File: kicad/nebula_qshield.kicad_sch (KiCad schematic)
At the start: 0 parts

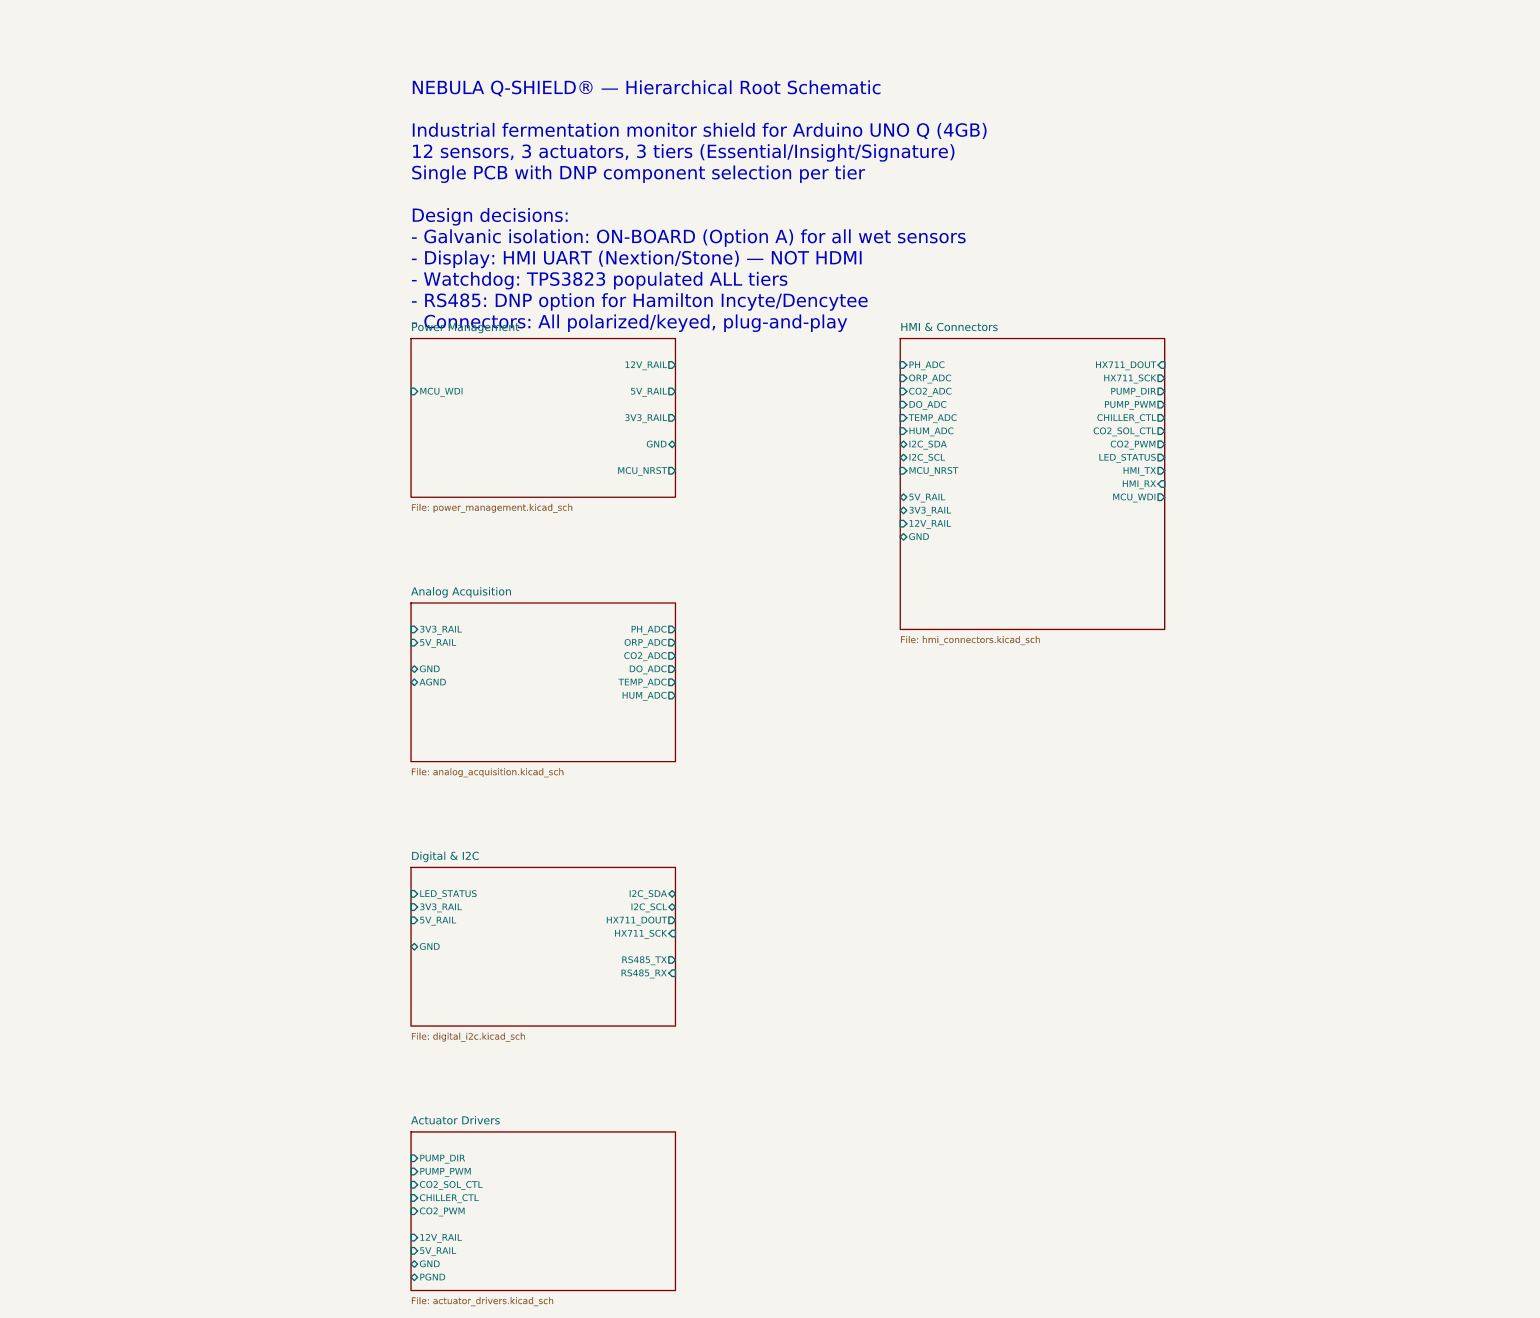
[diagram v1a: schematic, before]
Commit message: feat: Wire digital_i2c, actuator_drivers, hmi_connectors + root schematic — ERC violations 322→24 (acceptable)
Co-Authored-By: Devin AI <158243242+devin-ai-integration[bot]@users.noreply.github.com>
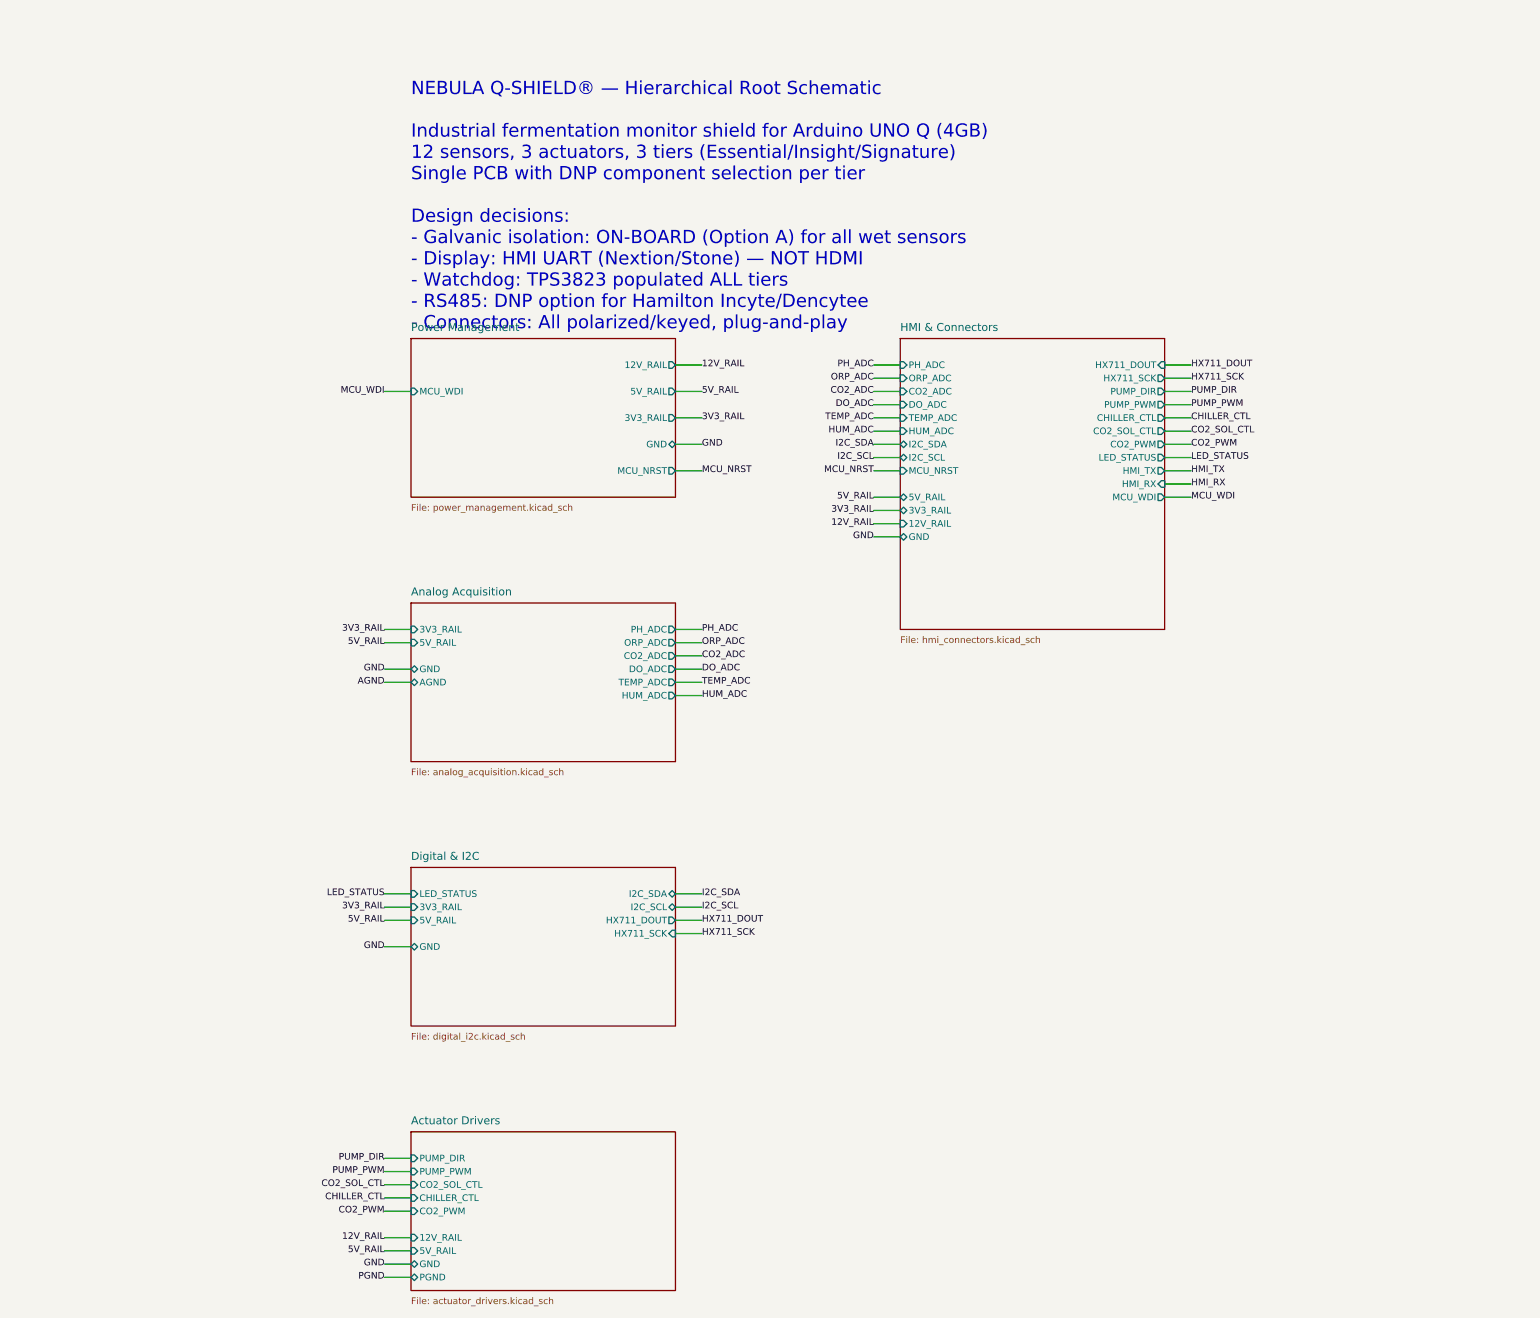
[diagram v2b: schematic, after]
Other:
- sheet Digital & I2C ports: added none; removed RS485_RX, RS485_TX
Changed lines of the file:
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@@
     (pin "HX711_SCK"  input       (at 76.2 165.1 0)     (effects (font (size 1.27 1.27))))
     (pin "LED_STATUS" input       (at 25.4 157.48 180)  (effects (font (size 1.27 1.27))))
-    (pin "RS485_TX"   output      (at 76.2 170.18 0)    (effects (font (size 1.27 1.27))))
-    (pin "RS485_RX"   input       (at 76.2 172.72 0)    (effects (font (size 1.27 1.27))))
     (pin "3V3_RAIL"   input       (at 25.4 160.02 180)  (effects (font (size 1.27 1.27))))
     (pin "5V_RAIL"    input       (at 25.4 162.56 180)  (effects (font (size 1.27 1.27))))
@@
     (effects (font (size 2.54 2.54)) (justify left))
   )
+  (wire (pts (xy 76.20 55.88) (xy 81.28 55.88)) (stroke (width 0) (type default)))
+  (label "12V_RAIL" (at 81.28 55.88 0) (effects (font (size 1.27 1.27))))
+  (wire (pts (xy 25.40 223.52) (xy 20.32 223.52)) (stroke (width 0) (type default)))
+  (label "12V_RAIL" (at 20.32 223.52 180) (effects (font (size 1.27 1.27))))
+  (wire (pts (xy 119.38 86.36) (xy 114.30 86.36)) (stroke (width 0) (type default)))
+  (label "12V_RAIL" (at 114.30 86.36 180) (effects (font (size 1.27 1.27))))
+  (wire (pts (xy 76.20 60.96) (xy 81.28 60.96)) (stroke (width 0) (type default)))
+  (label "5V_RAIL" (at 81.28 60.96 0) (effects (font (size 1.27 1.27))))
+  (wire (pts (xy 25.40 109.22) (xy 20.32 109.22)) (stroke (width 0) (type default)))
+  (label "5V_RAIL" (at 20.32 109.22 180) (effects (font (size 1.27 1.27))))
+  (wire (pts (xy 25.40 162.56) (xy 20.32 162.56)) (stroke (width 0) (type default)))
+  (label "5V_RAIL" (at 20.32 162.56 180) (effects (font (size 1.27 1.27))))
+  (wire (pts (xy 25.40 226.06) (xy 20.32 226.06)) (stroke (width 0) (type default)))
+  (label "5V_RAIL" (at 20.32 226.06 180) (effects (font (size 1.27 1.27))))
+  (wire (pts (xy 119.38 81.28) (xy 114.30 81.28)) (stroke (width 0) (type default)))
+  (label "5V_RAIL" (at 114.30 81.28 180) (effects (font (size 1.27 1.27))))
+  (wire (pts (xy 76.20 66.04) (xy 81.28 66.04)) (stroke (width 0) (type default)))
+  (label "3V3_RAIL" (at 81.28 66.04 0) (effects (font (size 1.27 1.27))))
+  (wire (pts (xy 25.40 106.68) (xy 20.32 106.68)) (stroke (width 0) (type default)))
+  (label "3V3_RAIL" (at 20.32 106.68 180) (effects (font (size 1.27 1.27))))
+  (wire (pts (xy 25.40 160.02) (xy 20.32 160.02)) (stroke (width 0) (type default)))
+  (label "3V3_RAIL" (at 20.32 160.02 180) (effects (font (size 1.27 1.27))))
+  (wire (pts (xy 119.38 83.82) (xy 114.30 83.82)) (stroke (width 0) (type default)))
+  (label "3V3_RAIL" (at 114.30 83.82 180) (effects (font (size 1.27 1.27))))
+  (wire (pts (xy 76.20 71.12) (xy 81.28 71.12)) (stroke (width 0) (type default)))
+  (label "GND" (at 81.28 71.12 0) (effects (font (size 1.27 1.27))))
+  (wire (pts (xy 25.40 114.30) (xy 20.32 114.30)) (stroke (width 0) (type default)))
+  (label "GND" (at 20.32 114.30 180) (effects (font (size 1.27 1.27))))
+  (wire (pts (xy 25.40 167.64) (xy 20.32 167.64)) (stroke (width 0) (type default)))
+  (label "GND" (at 20.32 167.64 180) (effects (font (size 1.27 1.27))))
+  (wire (pts (xy 25.40 228.60) (xy 20.32 228.60)) (stroke (width 0) (type default)))
+  (label "GND" (at 20.32 228.60 180) (effects (font (size 1.27 1.27))))
+  (wire (pts (xy 119.38 88.90) (xy 114.30 88.90)) (stroke (width 0) (type default)))
+  (label "GND" (at 114.30 88.90 180) (effects (font (size 1.27 1.27))))
+  (wire (pts (xy 25.40 231.14) (xy 20.32 231.14)) (stroke (width 0) (type default)))
+  (label "PGND" (at 20.32 231.14 180) (effects (font (size 1.27 1.27))))
+  (wire (pts (xy 25.40 116.84) (xy 20.32 116.84)) (stroke (width 0) (type default)))
+  (label "AGND" (at 20.32 116.84 180) (effects (font (size 1.27 1.27))))
+  (wire (pts (xy 76.20 106.68) (xy 81.28 106.68)) (stroke (width 0) (type default)))
+  (label "PH_ADC" (at 81.28 106.68 0) (effects (font (size 1.27 1.27))))
+  (wire (pts (xy 119.38 55.88) (xy 114.30 55.88)) (stroke (width 0) (type default)))
+  (label "PH_ADC" (at 114.30 55.88 180) (effects (font (size 1.27 1.27))))
+  (wire (pts (xy 76.20 109.22) (xy 81.28 109.22)) (stroke (width 0) (type default)))
+  (label "ORP_ADC" (at 81.28 109.22 0) (effects (font (size 1.27 1.27))))
+  (wire (pts (xy 119.38 58.42) (xy 114.30 58.42)) (stroke (width 0) (type default)))
+  (label "ORP_ADC" (at 114.30 58.42 180) (effects (font (size 1.27 1.27))))
+  (wire (pts (xy 76.20 111.76) (xy 81.28 111.76)) (stroke (width 0) (type default)))
+  (label "CO2_ADC" (at 81.28 111.76 0) (effects (font (size 1.27 1.27))))
+  (wire (pts (xy 119.38 60.96) (xy 114.30 60.96)) (stroke (width 0) (type default)))
+  (label "CO2_ADC" (at 114.30 60.96 180) (effects (font (size 1.27 1.27))))
+  (wire (pts (xy 76.20 114.30) (xy 81.28 114.30)) (stroke (width 0) (type default)))
+  (label "DO_ADC" (at 81.28 114.30 0) (effects (font (size 1.27 1.27))))
+  (wire (pts (xy 119.38 63.50) (xy 114.30 63.50)) (stroke (width 0) (type default)))
+  (label "DO_ADC" (at 114.30 63.50 180) (effects (font (size 1.27 1.27))))
+  (wire (pts (xy 76.20 116.84) (xy 81.28 116.84)) (stroke (width 0) (type default)))
+  (label "TEMP_ADC" (at 81.28 116.84 0) (effects (font (size 1.27 1.27))))
+  (wire (pts (xy 119.38 66.04) (xy 114.30 66.04)) (stroke (width 0) (type default)))
+  (label "TEMP_ADC" (at 114.30 66.04 180) (effects (font (size 1.27 1.27))))
+  (wire (pts (xy 76.20 119.38) (xy 81.28 119.38)) (stroke (width 0) (type default)))
+  (label "HUM_ADC" (at 81.28 119.38 0) (effects (font (size 1.27 1.27))))
+  (wire (pts (xy 119.38 68.58) (xy 114.30 68.58)) (stroke (width 0) (type default)))
+  (label "HUM_ADC" (at 114.30 68.58 180) (effects (font (size 1.27 1.27))))
+  (wire (pts (xy 76.20 157.48) (xy 81.28 157.48)) (stroke (width 0) (type default)))
+  (label "I2C_SDA" (at 81.28 157.48 0) (effects (font (size 1.27 1.27))))
+  (wire (pts (xy 119.38 71.12) (xy 114.30 71.12)) (stroke (width 0) (type default)))
+  (label "I2C_SDA" (at 114.30 71.12 180) (effects (font (size 1.27 1.27))))
+  (wire (pts (xy 76.20 160.02) (xy 81.28 160.02)) (stroke (width 0) (type default)))
+  (label "I2C_SCL" (at 81.28 160.02 0) (effects (font (size 1.27 1.27))))
+  (wire (pts (xy 119.38 73.66) (xy 114.30 73.66)) (stroke (width 0) (type default)))
+  (label "I2C_SCL" (at 114.30 73.66 180) (effects (font (size 1.27 1.27))))
+  (wire (pts (xy 76.20 162.56) (xy 81.28 162.56)) (stroke (width 0) (type default)))
+  (label "HX711_DOUT" (at 81.28 162.56 0) (effects (font (size 1.27 1.27))))
+  (wire (pts (xy 170.18 55.88) (xy 175.26 55.88)) (stroke (width 0) (type default)))
+  (label "HX711_DOUT" (at 175.26 55.88 0) (effects (font (size 1.27 1.27))))
+  (wire (pts (xy 76.20 165.10) (xy 81.28 165.10)) (stroke (width 0) (type default)))
+  (label "HX711_SCK" (at 81.28 165.10 0) (effects (font (size 1.27 1.27))))
+  (wire (pts (xy 170.18 58.42) (xy 175.26 58.42)) (stroke (width 0) (type default)))
+  (label "HX711_SCK" (at 175.26 58.42 0) (effects (font (size 1.27 1.27))))
+  (wire (pts (xy 170.18 60.96) (xy 175.26 60.96)) (stroke (width 0) (type default)))
+  (label "PUMP_DIR" (at 175.26 60.96 0) (effects (font (size 1.27 1.27))))
+  (wire (pts (xy 25.40 208.28) (xy 20.32 208.28)) (stroke (width 0) (type default)))
+  (label "PUMP_DIR" (at 20.32 208.28 180) (effects (font (size 1.27 1.27))))
+  (wire (pts (xy 170.18 63.50) (xy 175.26 63.50)) (stroke (width 0) (type default)))
+  (label "PUMP_PWM" (at 175.26 63.50 0) (effects (font (size 1.27 1.27))))
+  (wire (pts (xy 25.40 210.82) (xy 20.32 210.82)) (stroke (width 0) (type default)))
+  (label "PUMP_PWM" (at 20.32 210.82 180) (effects (font (size 1.27 1.27))))
+  (wire (pts (xy 170.18 68.58) (xy 175.26 68.58)) (stroke (width 0) (type default)))
+  (label "CO2_SOL_CTL" (at 175.26 68.58 0) (effects (font (size 1.27 1.27))))
+  (wire (pts (xy 25.40 213.36) (xy 20.32 213.36)) (stroke (width 0) (type default)))
+  (label "CO2_SOL_CTL" (at 20.32 213.36 180) (effects (font (size 1.27 1.27))))
+  (wire (pts (xy 170.18 66.04) (xy 175.26 66.04)) (stroke (width 0) (type default)))
+  (label "CHILLER_CTL" (at 175.26 66.04 0) (effects (font (size 1.27 1.27))))
+  (wire (pts (xy 25.40 215.90) (xy 20.32 215.90)) (stroke (width 0) (type default)))
+  (label "CHILLER_CTL" (at 20.32 215.90 180) (effects (font (size 1.27 1.27))))
+  (wire (pts (xy 170.18 71.12) (xy 175.26 71.12)) (stroke (width 0) (type default)))
+  (label "CO2_PWM" (at 175.26 71.12 0) (effects (font (size 1.27 1.27))))
+  (wire (pts (xy 25.40 218.44) (xy 20.32 218.44)) (stroke (width 0) (type default)))
+  (label "CO2_PWM" (at 20.32 218.44 180) (effects (font (size 1.27 1.27))))
+  (wire (pts (xy 170.18 73.66) (xy 175.26 73.66)) (stroke (width 0) (type default)))
+  (label "LED_STATUS" (at 175.26 73.66 0) (effects (font (size 1.27 1.27))))
+  (wire (pts (xy 25.40 157.48) (xy 20.32 157.48)) (stroke (width 0) (type default)))
+  (label "LED_STATUS" (at 20.32 157.48 180) (effects (font (size 1.27 1.27))))
+  (wire (pts (xy 170.18 81.28) (xy 175.26 81.28)) (stroke (width 0) (type default)))
+  (label "MCU_WDI" (at 175.26 81.28 0) (effects (font (size 1.27 1.27))))
+  (wire (pts (xy 25.40 60.96) (xy 20.32 60.96)) (stroke (width 0) (type default)))
+  (label "MCU_WDI" (at 20.32 60.96 180) (effects (font (size 1.27 1.27))))
+  (wire (pts (xy 76.20 76.20) (xy 81.28 76.20)) (stroke (width 0) (type default)))
+  (label "MCU_NRST" (at 81.28 76.20 0) (effects (font (size 1.27 1.27))))
+  (wire (pts (xy 119.38 76.20) (xy 114.30 76.20)) (stroke (width 0) (type default)))
+  (label "MCU_NRST" (at 114.30 76.20 180) (effects (font (size 1.27 1.27))))
+  (wire (pts (xy 170.18 76.20) (xy 175.26 76.20)) (stroke (width 0) (type default)))
+  (label "HMI_TX" (at 175.26 76.20 0) (effects (font (size 1.27 1.27))))
+  (wire (pts (xy 170.18 78.74) (xy 175.26 78.74)) (stroke (width 0) (type default)))
+  (label "HMI_RX" (at 175.26 78.74 0) (effects (font (size 1.27 1.27))))
 )
